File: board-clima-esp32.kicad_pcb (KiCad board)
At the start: 2 copper layers, 76.2 x 64.3 mm, 54 parts, among them IC1 ESP32-S3-WROOM-1-N4, J1 Conn_01x06_Pin, J2 Screw_Terminal_01x03, J3 Conn_01x04_Pin, J5 Conn_01x05_Pin, J6 USB_C_Receptacle, Q1 AO3400A, Q2 AO3401A, Q3 AO3400A, SW1 RESET, SW2 BOOT, U1 AMS1117-3.3, U3 PC817, U4 PC817

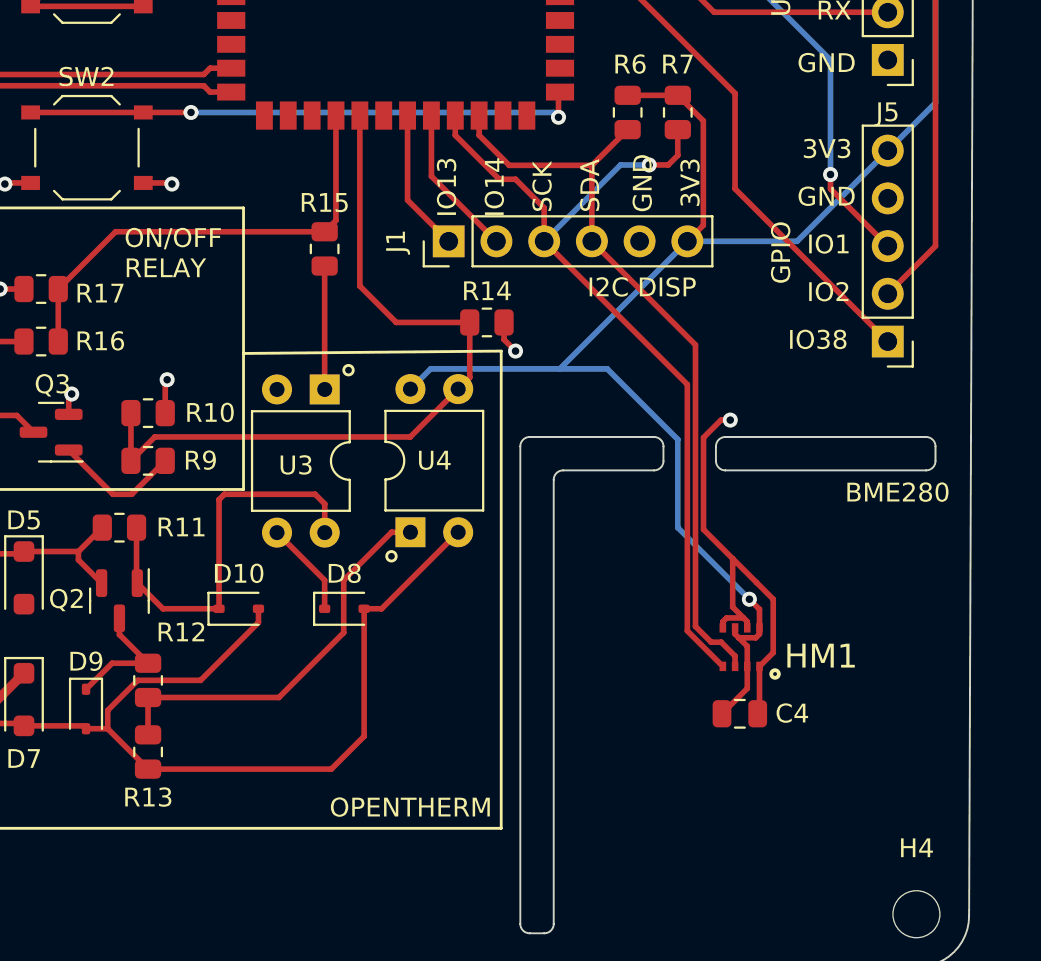
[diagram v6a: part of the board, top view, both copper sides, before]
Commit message: Moved BME and DISP connector
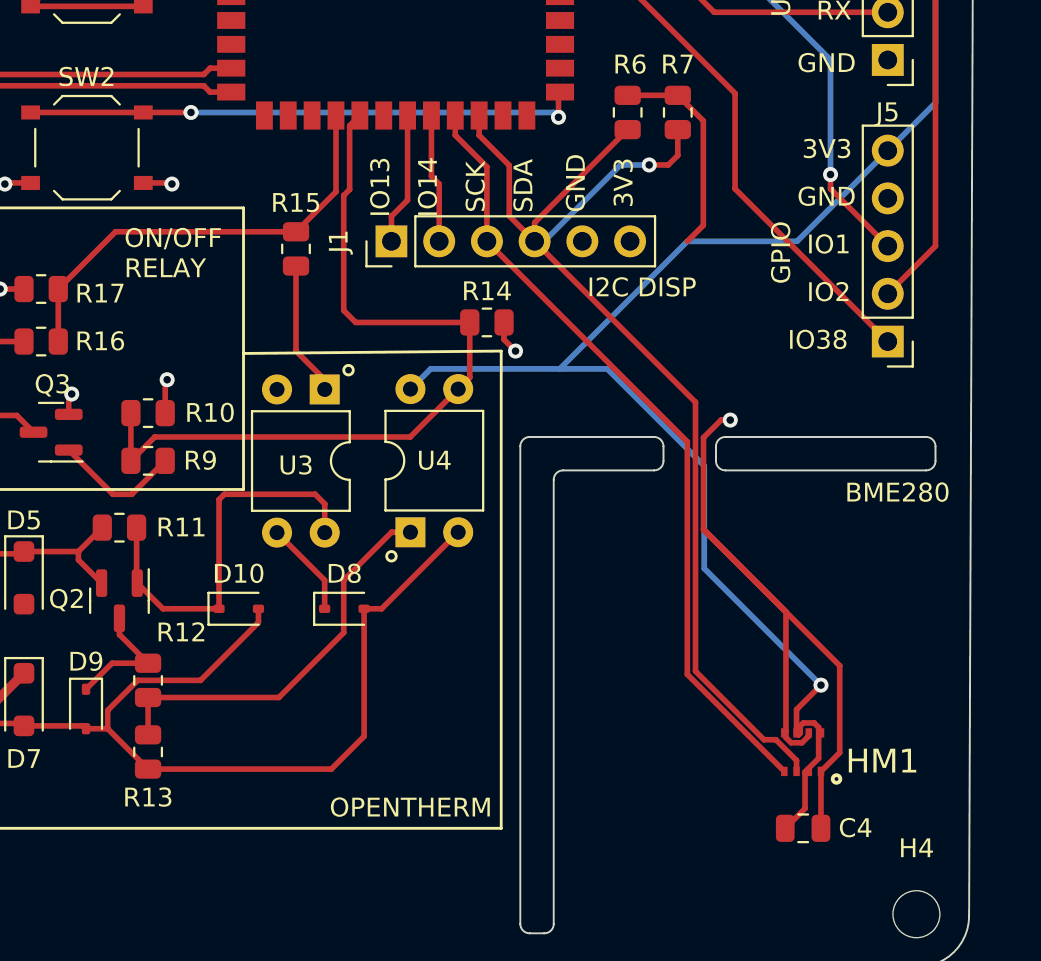
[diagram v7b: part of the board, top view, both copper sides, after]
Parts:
- moved C4 6.96 mm to (194.6, 180.3)
- moved HM1 6.48 mm to (195.6, 175.3)
- moved J1 3.05 mm to (172.7, 149.1)
- moved R15 1.52 mm to (167.6, 149.5)
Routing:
- net GND: track 86.8 -> 105.3 mm
- net /SDA: track 40.5 -> 50.3 mm
- net +3.3V: track 158.2 -> 166.7 mm
- net /SCK: track 46.1 -> 52.5 mm
- net /BOILER_2: track 41.1 -> 43.0 mm
- net /DISP_RST: track 8.13 -> 6.86 mm
- net /BOILER_1: track 24.7 -> 23.8 mm
- net Net-(R15-Pad1): track 6.57 -> 7.20 mm
- net /DISP_BUSY: track 7.60 -> 7.05 mm

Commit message: drc passes
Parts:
- added D11: LED, LED_SMD:LED_0805_2012Metric, F.Cu at (186.2, 136.9)
- added R18: 220, Resistor_SMD:R_0805_2012Metric, F.Cu at (189.2, 137.7)
- U2: moved to F.Cu
- moved U2 10.2 mm to (147.3, 154.7)
- moved J6 1.64 mm to (128.0, 138.9)
- moved H1 1.52 mm to (128.8, 126.2)
- moved H3 1.52 mm to (128.8, 184.9)
- moved HM1 0.09 mm to (195.7, 175.3)
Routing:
- net /R_NO: track 33.8 -> 46.8 mm
- net GND: track 105.3 -> 117.3 mm, vias 26 -> 33
- net Net-(D2-A): track 8.04 -> 16.9 mm, vias 0 -> 1
- net /R_NC: track 16.5 -> 8.04 mm
- net /GPIO3: track 28.0 -> 33.9 mm
- net Net-(D1-A): track 6.69 -> 12.1 mm, vias 0 -> 1
- net /GPIO2: track 43.4 -> 38.2 mm, vias 0 -> 2
- net Net-(D2-K): track 19.8 -> 14.8 mm
- net /GPIO1: track 30.6 -> 35.0 mm
- net +3.3V: track 166.7 -> 170.3 mm, vias 3 -> 4
- net /SCK: track 52.5 -> 55.6 mm
- net Net-(D3-A): track 0.00 -> 2.30 mm
- net Net-(D11-K): track 0.00 -> 2.21 mm
- net Net-(J6-CC2): track 3.20 -> 4.84 mm
- net Net-(J6-CC1): track 3.18 -> 4.82 mm
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- added copper zone on F.Cu, net GND
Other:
- board size 76.2 x 64.3 mm -> 77.7 x 64.3 mm
- board text added: "COM OT2"
- board text added: "NO OT1"
- board text added: "USR LED"
- board text removed: "COM/ OT2"
- board text removed: "NO/ OT1"
